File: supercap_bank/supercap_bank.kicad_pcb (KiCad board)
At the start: 4 copper layers, 12.2 x 54.6 mm, 12 parts, among them J10 FTSH-102-04-L-DH, J6 FTSH-102-04-L-DH, J7 FTSH-102-04-L-DH, J8 FTSH-102-04-L-DH, J9 FTSH-102-04-L-DH

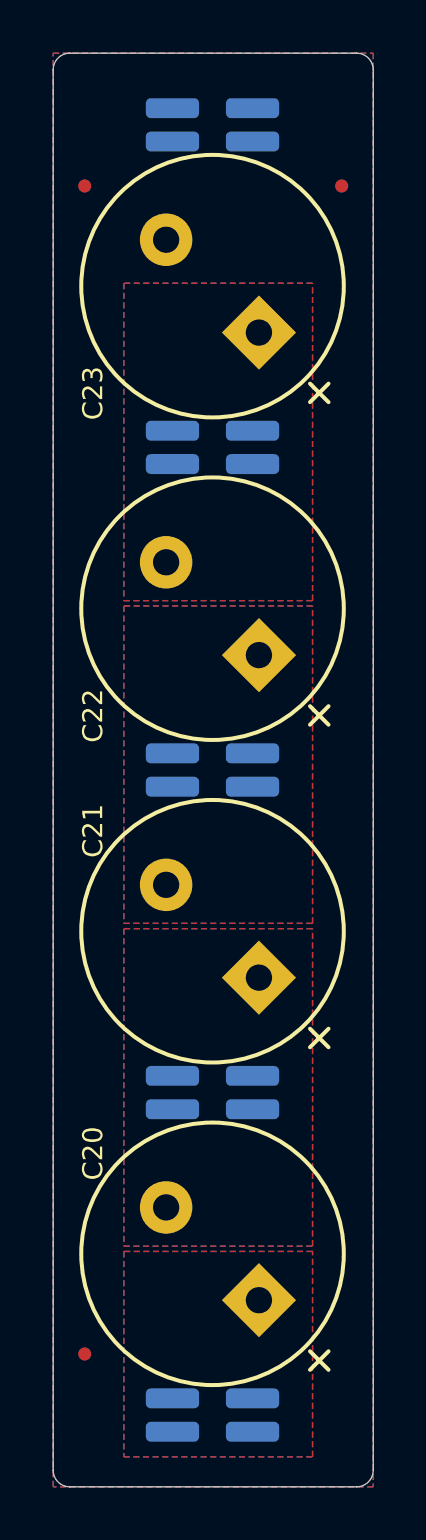
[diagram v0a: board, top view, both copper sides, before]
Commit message: Update KiCAD configuration and project files
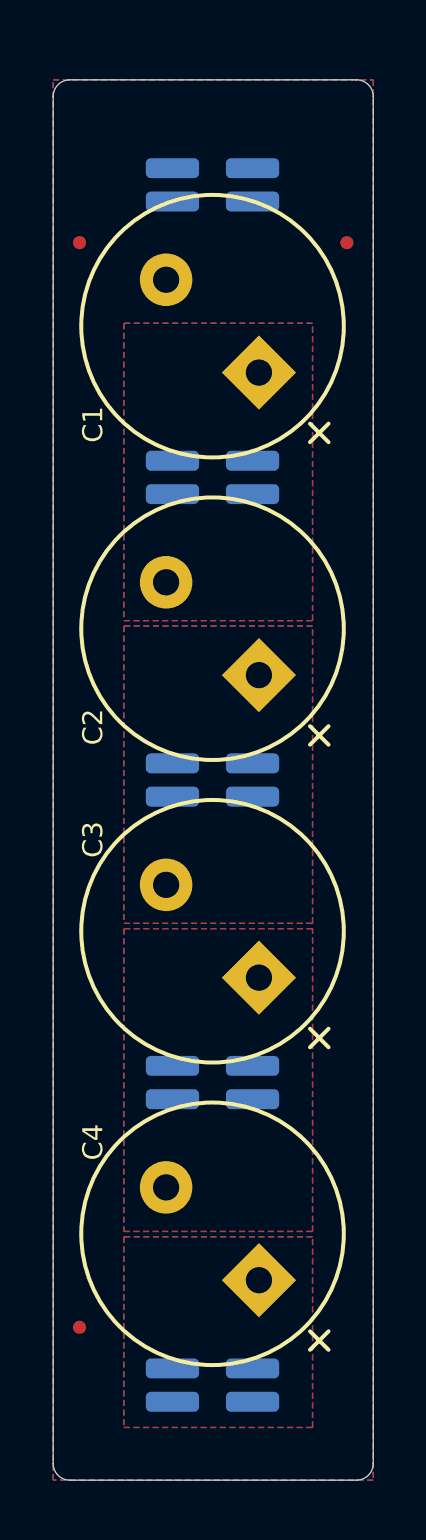
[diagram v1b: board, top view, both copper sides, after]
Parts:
- moved J1 2.29 mm to (134.9, 69.2)
- moved FID1 2.17 mm to (129.8, 71.4)
- moved FID2 2.17 mm to (140.0, 71.4)
- moved C1 1.52 mm to (134.9, 74.6)
- moved J5 1.14 mm to (134.9, 114.9)
- moved J2 1.14 mm to (134.9, 80.3)
- moved FID3 1.04 mm to (129.8, 112.7)
- moved C2 0.76 mm to (134.9, 86.1)
- moved C4 0.76 mm to (134.9, 109.2)
- moved J3 0.38 mm to (134.9, 91.9)
- moved J4 0.38 mm to (134.9, 103.4)
- renumbered C23 to C1, C22 to C2, C21 to C3, C20 to C4, FID2 to FID1, FID3 to FID2, FID1 to FID3, J10 to J1, J9 to J2, J8 to J3, J7 to J4, J6 to J5
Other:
- board size 12.2 x 54.6 mm -> 12.2 x 53.3 mm
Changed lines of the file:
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@@
 	(footprint "no_components_footprints:Fiducial_0.5mm_Mask1mm"
 		(layer "F.Cu")
-		(at 130.030787 69.245535)
+		(at 129.832667 71.404535)
 		(descr "Circular Fiducial, 0.5mm bare copper, 1mm soldermask opening (Level C)")
 		(tags "fiducial")
-		(property "Reference" "FID2"
+		(property "Reference" "FID1"
 			(at 0 -1.45 0)
 			(layer "F.SilkS")
@@
 			(fill no)
 			(layer "F.CrtYd")
-			(net 58)
 		)
 		(fp_circle
@@
 			(fill no)
 			(layer "F.Fab")
-			(net 58)
 		)
 		(fp_text user "${REFERENCE}"
@@
 	(footprint "capacitor_footprints:C_197x394_H31_5_5_0x10Metric"
 		(layer "F.Cu")
-		(at 134.8994 109.91992 135)
-		(property "Reference" "C20"
+		(at 134.8994 109.15792 135)
+		(property "Reference" "C4"
 			(at 5.511189 -1.559878 90)
 			(unlocked yes)
@@
 			)
 			(layer "F.SilkS")
-			(net 58)
 		)
 		(fp_line
@@
 			)
 			(layer "F.SilkS")
-			(net 58)
 		)
 		(fp_circle
@@
 			(fill no)
 			(layer "F.SilkS")
-			(net 58)
 		)
 		(fp_circle
@@
 			(fill no)
 			(layer "F.CrtYd")
-			(net 58)
 		)
 		(fp_line
@@
 			)
 			(layer "F.Fab")
-			(net 58)
 		)
 		(fp_line
@@
 			)
 			(layer "F.Fab")
-			(net 58)
 		)
 		(fp_circle
@@
 			(fill no)
 			(layer "F.Fab")
-			(net 58)
 		)
 		(fp_text user "${REFERENCE}"
@@
 	(footprint "no_components_footprints:Fiducial_0.5mm_Mask1mm"
 		(layer "F.Cu")
-		(at 130.030787 113.734945)
+		(at 129.832667 112.718945)
 		(descr "Circular Fiducial, 0.5mm bare copper, 1mm soldermask opening (Level C)")
 		(tags "fiducial")
-		(property "Reference" "FID1"
+		(property "Reference" "FID3"
 			(at 0 -1.45 0)
 			(layer "F.SilkS")
@@
 			(fill no)
 			(layer "F.CrtYd")
-			(net 58)
 		)
 		(fp_circle
@@
 			(fill no)
 			(layer "F.Fab")
-			(net 58)
 		)
 		(fp_text user "${REFERENCE}"
@@
 		(layer "F.Cu")
 		(at 134.8994 97.63267 135)
-		(property "Reference" "C21"
+		(property "Reference" "C3"
 			(at 5.511189 -1.559878 90)
 			(unlocked yes)
@@
 			)
 			(layer "F.SilkS")
-			(net 58)
 		)
 		(fp_line
@@
 			)
 			(layer "F.SilkS")
-			(net 58)
 		)
 		(fp_circle
@@
 			(fill no)
 			(layer "F.SilkS")
-			(net 58)
 		)
 		(fp_circle
@@
 			(fill no)
 			(layer "F.CrtYd")
-			(net 58)
 		)
 		(fp_line
@@
 			)
 			(layer "F.Fab")
-			(net 58)
 		)
 		(fp_line
@@
 			)
 			(layer "F.Fab")
-			(net 58)
 		)
 		(fp_circle
@@
 			(fill no)
 			(layer "F.Fab")
-			(net 58)
 		)
 		(fp_text user "${REFERENCE}"
@@
 	(footprint "capacitor_footprints:C_197x394_H31_5_5_0x10Metric"
 		(layer "F.Cu")
-		(at 134.8994 73.06056 135)
-		(property "Reference" "C23"
+		(at 134.8994 74.58456 135)
+		(property "Reference" "C1"
 			(at 1.380272 -5.690795 90)
 			(unlocked yes)
@@
 			)
 			(layer "F.SilkS")
-			(net 58)
 		)
 		(fp_line
@@
 			)
 			(layer "F.SilkS")
-			(net 58)
 		)
 		(fp_circle
@@
 			(fill no)
 			(layer "F.SilkS")
-			(net 58)
 		)
 		(fp_circle
@@
 			(fill no)
 			(layer "F.CrtYd")
-			(net 58)
 		)
 		(fp_line
@@
 			)
 			(layer "F.Fab")
-			(net 58)
 		)
 		(fp_line
@@
 			)
 			(layer "F.Fab")
-			(net 58)
 		)
 		(fp_circle
@@
 			(fill no)
 			(layer "F.Fab")
-			(net 58)
 		)
 		(fp_text user "${REFERENCE}"
@@
 	(footprint "capacitor_footprints:C_197x394_H31_5_5_0x10Metric"
 		(layer "F.Cu")
-		(at 134.8994 85.34669 135)
-		(property "Reference" "C22"
+		(at 134.8994 86.10869 135)
+		(property "Reference" "C2"
 			(at 1.380271 -5.690795 90)
 			(unlocked yes)
@@
 			)
 			(layer "F.SilkS")
-			(net 58)
 		)
 		(fp_line
@@
 			)
 			(layer "F.SilkS")
-			(net 58)
 		)
 		(fp_circle
@@
 			(fill no)
 			(layer "F.SilkS")
-			(net 58)
 		)
 		(fp_circle
@@
 			(fill no)
 			(layer "F.CrtYd")
-			(net 58)
 		)
 		(fp_line
@@
 			)
 			(layer "F.Fab")
-			(net 58)
 		)
 		(fp_line
@@
 			)
 			(layer "F.Fab")
-			(net 58)
 		)
 		(fp_circle
@@
 			(fill no)
 			(layer "F.Fab")
-			(net 58)
 		)
 		(fp_text user "${REFERENCE}"
@@
 	(footprint "no_components_footprints:Fiducial_0.5mm_Mask1mm"
 		(layer "F.Cu")
-		(at 139.818813 69.245535)
+		(at 140.016933 71.404535)
 		(descr "Circular Fiducial, 0.5mm bare copper, 1mm soldermask opening (Level C)")
 		(tags "fiducial")
-		(property "Reference" "FID3"
+		(property "Reference" "FID2"
 			(at 0 -1.45 0)
 			(layer "F.SilkS")
@@
 			(fill no)
 			(layer "F.CrtYd")
-			(net 58)
 		)
 		(fp_circle
@@
 			(fill no)
 			(layer "F.Fab")
-			(net 58)
 		)
 		(fp_text user "${REFERENCE}"
@@
 	(footprint "connector_footprints:FTSH-102-04-L-DH"
 		(layer "B.Cu")
-		(at 134.8984 116.06276 -90)
-		(property "Reference" "J6"
+		(at 134.8984 114.91976 -90)
+		(property "Reference" "J5"
 			(at 0 -3 0)
 			(unlocked yes)
@@
 	(footprint "connector_footprints:FTSH-102-04-L-DH"
 		(layer "B.Cu")
-		(at 134.8984 79.20355 -90)
-		(property "Reference" "J9"
+		(at 134.8984 80.34655 -90)
+		(property "Reference" "J2"
 			(at 0 -3 0)
 			(unlocked yes)
@@
 	(footprint "connector_footprints:FTSH-102-04-L-DH"
 		(layer "B.Cu")
-		(at 134.8984 66.9163 -90)
-		(property "Reference" "J10"
+		(at 134.8984 69.2023 -90)
+		(property "Reference" "J1"
 			(at 0 -3 0)
 			(unlocked yes)
@@
 	(footprint "connector_footprints:FTSH-102-04-L-DH"
 		(layer "B.Cu")
-		(at 134.8984 91.4908 -90)
-		(property "Reference" "J8"
+		(at 134.8984 91.8718 -90)
+		(property "Reference" "J3"
 			(at 0 -3 0)
 			(unlocked yes)
@@
 	(footprint "connector_footprints:FTSH-102-04-L-DH"
 		(layer "B.Cu")
-		(at 134.8984 103.776575 -90)
-		(property "Reference" "J7"
+		(at 134.8984 103.395575 -90)
+		(property "Reference" "J4"
 			(at 0 -3 0)
 			(unlocked yes)
@@
 	)
 	(gr_arc
-		(start 140.3858 64.1858)
-		(mid 140.834813 64.371787)
-		(end 141.0208 64.8208)
+		(start 140.3858 65.2018)
+		(mid 140.834813 65.387787)
+		(end 141.0208 65.8368)
 		(stroke
 			(width 0.05)
@@
 	)
 	(gr_arc
-		(start 141.0208 118.1608)
-		(mid 140.834813 118.609813)
-		(end 140.3858 118.7958)
+		(start 141.0208 117.9068)
+		(mid 140.834813 118.355813)
+		(end 140.3858 118.5418)
 		(stroke
 			(width 0.05)
@@
 	)
 	(gr_line
-		(start 128.8288 118.1608)
-		(end 128.8288 64.8208)
+		(start 128.8288 117.9068)
+		(end 128.8288 65.8368)
 		(stroke
 			(width 0.05)
@@
 	)
 	(gr_arc
-		(start 128.8288 64.8208)
-		(mid 129.014787 64.371787)
-		(end 129.4638 64.1858)
+		(start 128.8288 65.8368)
+		(mid 129.014787 65.387787)
+		(end 129.4638 65.2018)
 		(stroke
 			(width 0.05)
@@
 	)
 	(gr_line
-		(start 140.3858 118.7958)
-		(end 129.4638 118.7958)
+		(start 140.3858 118.5418)
+		(end 129.4638 118.5418)
 		(stroke
 			(width 0.05)
@@
 	)
 	(gr_line
-		(start 129.4638 64.1858)
-		(end 140.3858 64.1858)
+		(start 129.4638 65.2018)
+		(end 140.3858 65.2018)
 		(stroke
 			(width 0.05)
@@
 	)
 	(gr_line
-		(start 141.0208 64.8208)
-		(end 141.0208 118.1608)
+		(start 141.0208 65.8368)
+		(end 141.0208 117.9068)
 		(stroke
 			(width 0.05)
@@
 	)
 	(gr_arc
-		(start 129.4638 118.7958)
-		(mid 129.014787 118.609813)
-		(end 128.8288 118.1608)
+		(start 129.4638 118.5418)
+		(mid 129.014787 118.355813)
+		(end 128.8288 117.9068)
 		(stroke
 			(width 0.05)
@@
 		(polygon
 			(pts
-				(xy 138.7094 109.8296) (xy 131.5212 109.8296) (xy 131.5212 117.6528) (xy 138.7094 117.6528)
+				(xy 138.7094 109.2708) (xy 131.5212 109.2708) (xy 131.5212 116.5352) (xy 138.7094 116.5352)
 			)
 		)
@@
 		(polygon
 			(pts
-				(xy 131.5212 85.2424) (xy 131.5212 97.3328) (xy 138.7094 97.3328) (xy 138.7094 85.2424)
+				(xy 131.5212 86.0044) (xy 131.5212 97.3328) (xy 138.7094 97.3328) (xy 138.7094 86.0044)
 			)
 		)
@@
 		(polygon
 			(pts
-				(xy 138.7094 72.9488) (xy 131.5212 72.9488) (xy 131.5212 85.0392) (xy 138.7094 85.0392)
+				(xy 138.7094 74.4728) (xy 131.5212 74.4728) (xy 131.5212 85.8012) (xy 138.7094 85.8012)
 			)
 		)
@@
 		(polygon
 			(pts
-				(xy 131.5212 97.536) (xy 131.5212 109.6264) (xy 138.7094 109.6264) (xy 138.7094 97.536)
+				(xy 131.5212 97.536) (xy 131.5212 109.0676) (xy 138.7094 109.0676) (xy 138.7094 97.536)
 			)
 		)
@@
 		(polygon
 			(pts
-				(xy 141.0208 64.1858) (xy 141.0208 118.7958) (xy 128.8288 118.7958) (xy 128.8288 64.1858)
+				(xy 141.0208 65.2018) (xy 141.0208 118.5418) (xy 128.8288 118.5418) (xy 128.8288 65.2018)
 			)
 		)

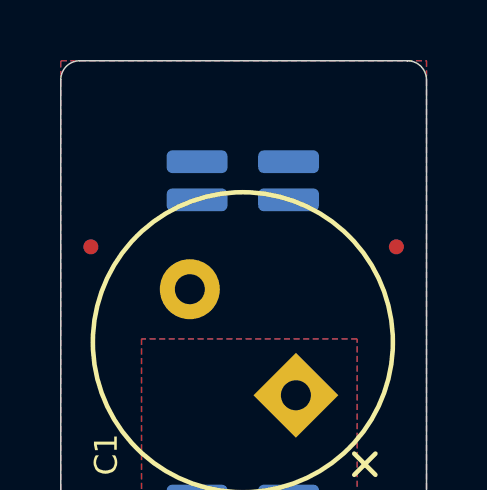
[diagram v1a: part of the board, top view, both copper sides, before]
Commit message: Update KiCAD project files and submodule
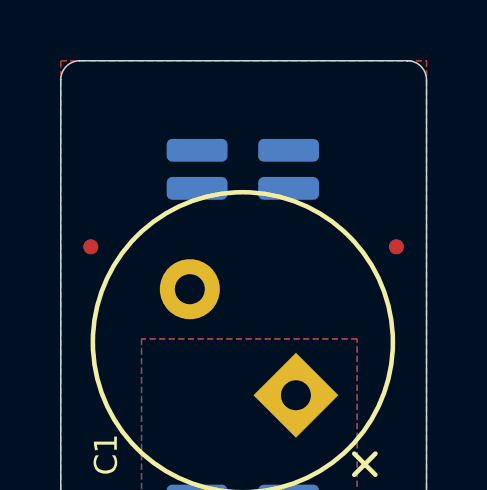
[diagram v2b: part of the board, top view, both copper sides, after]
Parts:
- moved J1 0.38 mm to (134.9, 68.8)
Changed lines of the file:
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@@
 	(footprint "connector_footprints:FTSH-102-04-L-DH"
 		(layer "B.Cu")
-		(at 134.8984 69.2023 -90)
+		(at 134.8984 68.8213 -90)
 		(property "Reference" "J1"
 			(at 0 -3 0)
